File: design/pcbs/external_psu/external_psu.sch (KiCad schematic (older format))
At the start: 41 parts, among them J1 IEC 320-C14 socket, J2 DIN-4

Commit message: Updated PCB sheet info. Clarified licence in readme.
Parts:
- removed J1: IEC 320-C14 socket, symbol Connector_Generic:Conn_01x03
- removed J2: DIN-4, symbol Connector:DIN-4
- FB1: Done (none) -> Yes
- PS2: DigiKey (none) -> 945-3441-ND; Done (none) -> Yes
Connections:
- no-connect marks 3 -> 4
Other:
- note removed: "TODO: Add bushing\n(https://www.digikey.com.au/products/en/cables-wires-management/bushings-grommets/491?k=&pkeyword=&sv=0&pv716=10753&pv716=10888&pv716=12091&pv716=13319&sf=0&FV=845%7C323848%2C-8%7C491&quantity=&ColumnSort=1000011&page=1&stock=1&nstock=1&pageSize=25)\n\nAdd spiral wrap / techflex"
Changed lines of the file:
@@
 F 1 "RAC03-05SK" H 3150 5424 50  0000 C CNN
 F 2 "CONV_RAC03-05SK" H 2850 4550 50  0001 L BNN
-F 3 "Unavailable" H 3000 4400 50  0001 L BNN
+F 3 "https://www.recom-power.com/pdf/Powerline_AC-DC/RAC03-K.pdf" H 3000 4400 50  0001 L BNN
+F 4 "945-3441-ND" H 3150 5050 50  0001 C CNN "DigiKey"
+F 5 "Yes" H 3150 5050 50  0001 C CNN "Done"
 	1    3150 5050
 	1    0    0    -1
@@
 	7800 3550 7550 3550
 $Comp
-L Connector_Generic:Conn_01x03 J1
+L Connector_Generic:Conn_01x03 #J1
 U 1 1 5ED1F0ED
 P 1050 3550
-F 0 "J1" H 968 3867 50  0000 C CNN
+F 0 "#J1" H 968 3867 50  0000 C CNN
 F 1 "IEC 320-C14 socket" H 968 3776 50  0000 C CNN
 F 2 "" H 1050 3550 50  0001 C CNN
@@
 NoConn ~ 9850 4500
 NoConn ~ 9550 4500
-$Comp
-L Connector:DIN-4 J2
-U 1 1 5EED7BCF
-P 10350 4250
-F 0 "J2" V 10304 4020 50  0000 R CNN
-F 1 "DIN-4" V 10395 4020 50  0000 R CNN
-F 2 "" H 10350 4250 50  0001 C CNN
-F 3 "https://domino2.kycon.com/website/Tools/assemblyvideos/KPPX/KPPX%20Assembly%20instruction.pdf" H 10350 4250 50  0001 C CNN
-F 4 "2092-KPPX-4P-ND" V 10350 4250 50  0001 C CNN "DigiKey"
-	1    10350 4250
-	0    -1   1    0
-$EndComp
 Text Notes 9350 4900 0    50   ~ 0
 Ferrite bead around power \ncable on DAC end
@@
 	7400 3250 7800 3250
 Wire Wire Line
-	10050 4150 10050 4250
-Wire Wire Line
-	10050 4350 10050 4300
-Wire Wire Line
-	10350 3950 10000 3950
-Wire Wire Line
-	10000 3950 10000 4200
-Wire Wire Line
 	8350 3350 7800 3350
 Wire Wire Line
@@
 Wire Wire Line
 	7800 3250 7850 3250
-Wire Wire Line
-	10350 4550 10000 4550
-Wire Wire Line
-	10000 4550 10000 4350
 $Comp
 L Device:Ferrite_Bead FB1
@@
 F 3 "~" H 9700 4500 50  0001 C CNN
 F 4 "240-2497-ND" H 9700 4500 50  0001 C CNN "DigiKey"
+F 5 "Yes" H 9700 4500 50  0001 C CNN "Done"
 	1    9700 4500
 	0    1    1    0
 $EndComp
 Wire Wire Line
-	7550 3550 7550 4250
-Wire Wire Line
-	8350 4200 10000 4200
-Wire Wire Line
-	8350 3350 8350 4200
-Wire Wire Line
-	7800 4300 10050 4300
-Wire Wire Line
-	7400 3850 7800 3850
-Wire Wire Line
-	10050 4250 7550 4250
-Connection ~ 7550 4250
-Wire Wire Line
-	7550 4250 7550 5250
-Wire Wire Line
 	7400 4850 7800 4850
-Wire Wire Line
-	7800 4300 7800 3850
-Connection ~ 7800 3850
-Wire Wire Line
-	7800 3850 7850 3850
 Wire Wire Line
 	7800 4350 7800 4850
@@
 Text Notes 1150 2750 0    50   ~ 0
 Enclosure
-Text Notes 8250 5400 0    50   ~ 0
-TODO: Add bushing\n(https://www.digikey.com.au/products/en/cables-wires-management/bushings-grommets/491?k=&pkeyword=&sv=0&pv716=10753&pv716=10888&pv716=12091&pv716=13319&sf=0&FV=845%7C323848%2C-8%7C491&quantity=&ColumnSort=1000011&page=1&stock=1&nstock=1&pageSize=25)\n\nAdd spiral wrap / techflex
+$Comp
+L Connector:XLR5 #J2
+U 1 1 5EF8330A
+P 10350 4250
+F 0 "#J2" V 10396 4478 50  0000 L CNN
+F 1 "XLR5" V 10305 4478 50  0000 L CNN
+F 2 "" H 10350 4250 50  0001 C CNN
+F 3 "http://ioaudiotech.com/datasheet/IO-XLR5-BK.pdf" H 10350 4250 50  0001 C CNN
+F 4 "1937-1035-ND" V 10350 4250 50  0001 C CNN "DigiKey"
+F 5 "Yes" V 10350 4250 50  0001 C CNN "Done"
+	1    10350 4250
+	0    1    -1   0
+$EndComp
+Wire Wire Line
+	10000 4600 10350 4600
+Wire Wire Line
+	10350 4600 10350 4550
+Wire Wire Line
+	10000 4350 10000 4600
+Wire Wire Line
+	10250 4550 10050 4550
+Wire Wire Line
+	10050 4550 10050 4300
+Connection ~ 7550 4300
+Wire Wire Line
+	7550 4300 7550 5250
+Wire Wire Line
+	7550 3550 7550 4300
+Wire Wire Line
+	7550 4300 10050 4300
+Wire Wire Line
+	7400 3850 7800 3850
+Wire Wire Line
+	10050 4250 8350 4250
+Wire Wire Line
+	8350 3350 8350 4250
+Wire Wire Line
+	10250 3950 10050 3950
+Wire Wire Line
+	10050 3950 10050 4200
+Wire Wire Line
+	10050 4200 7800 4200
+Wire Wire Line
+	7800 4200 7800 3850
+Connection ~ 7800 3850
+Wire Wire Line
+	7800 3850 7850 3850
+NoConn ~ 10350 3950
 $EndSCHEMATC

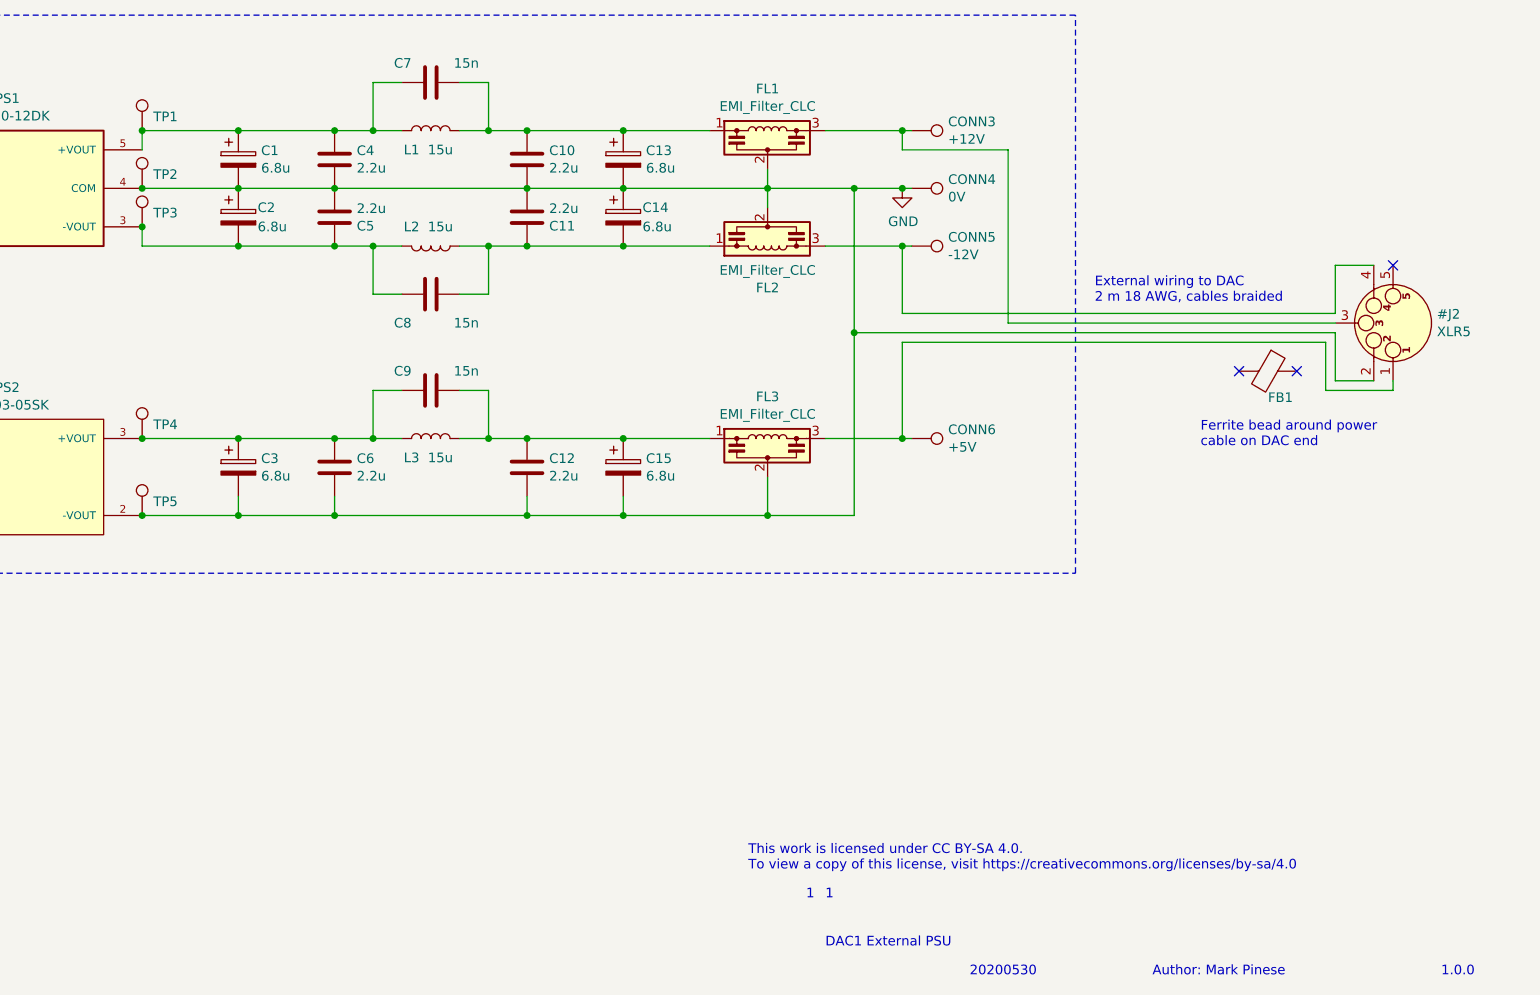
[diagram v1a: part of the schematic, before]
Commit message: Fixed title blocks. Added fab outputs.
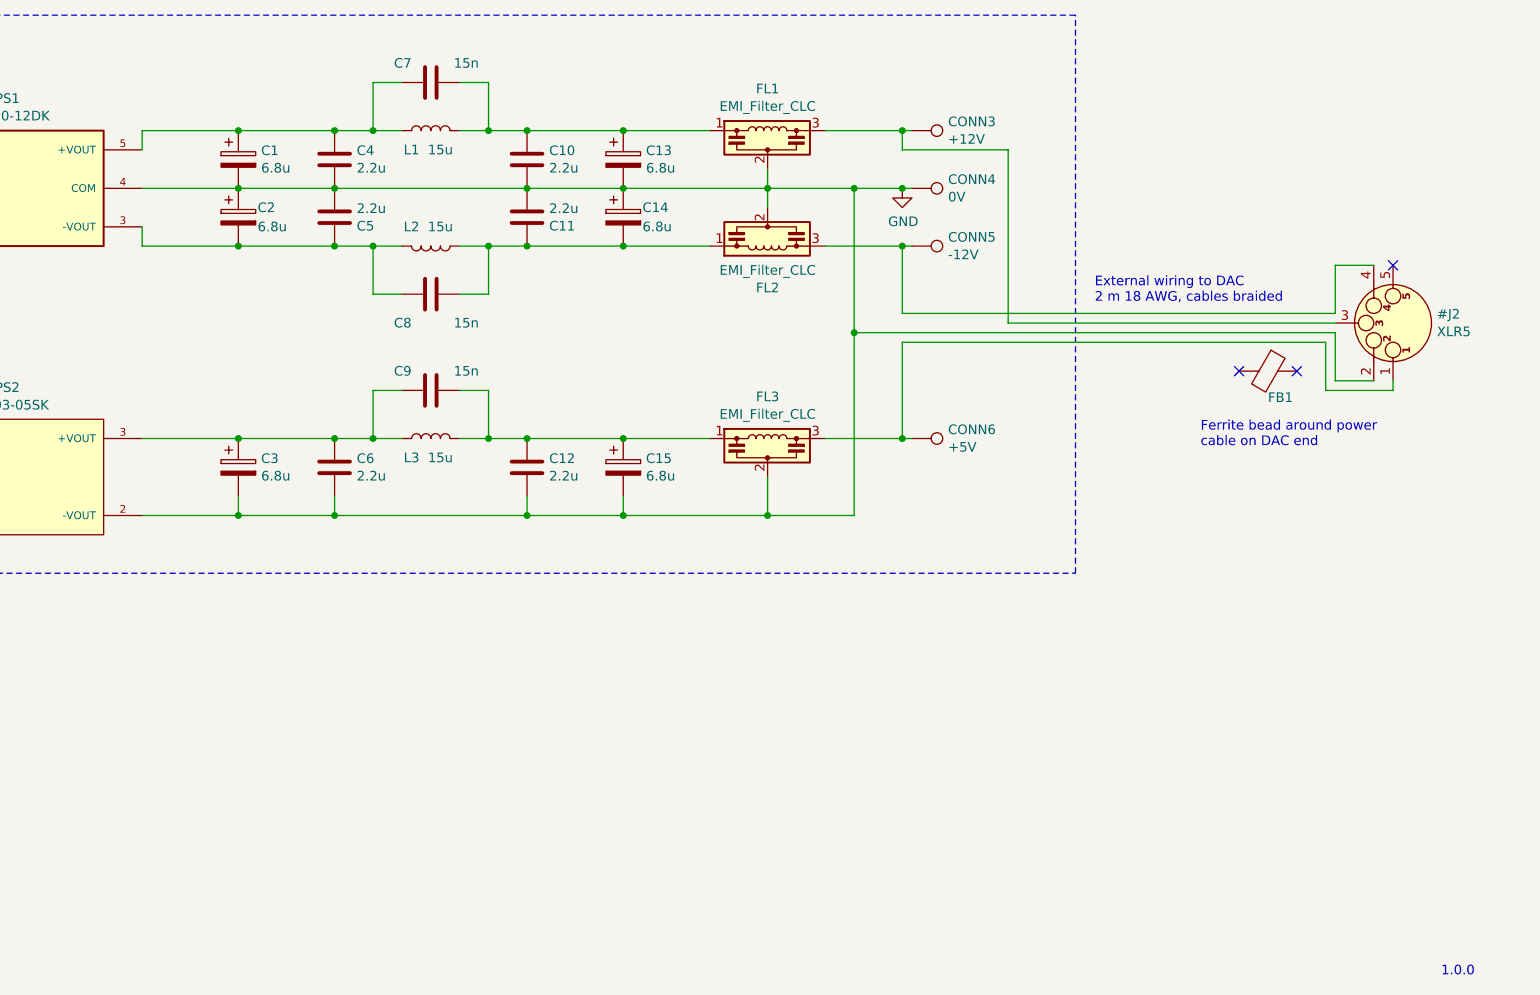
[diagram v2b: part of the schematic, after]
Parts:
- removed TP1, TP2, TP3, TP4, TP5: TestPoint, TestPoint:TestPoint_Pad_2.0x2.0mm, symbol Connector:TestPoint
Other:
- note removed: "1"
- note removed: "20200530"
- note removed: "Author: Mark Pinese"
- note removed: "DAC1 External PSU"
- note removed: "This work is licensed under CC BY-SA 4.0.\nTo view a copy of this license, visit https://creativecommons.org/licenses/by-sa/4.0"
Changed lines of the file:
@@
 encoding utf-8
 Sheet 1 1
-Title ""
-Date ""
-Rev ""
-Comp ""
-Comment1 ""
-Comment2 ""
+Title "DAC1 External PSU"
+Date "2020-06-27"
+Rev "1.0.0"
+Comp "© Mark Pinese 2020"
+Comment1 "To view a copy of this license, visit https://creativecommons.org/licenses/by/4.0"
+Comment2 "This work is licensed under CC BY 4.0."
 Comment3 ""
 Comment4 ""
@@
 	0    -1   -1   0
 $EndComp
-Text Notes 7400 7500 0    50   ~ 0
-DAC1 External PSU
 Text Notes 10600 7650 0    50   ~ 0
 1.0.0
-Text Notes 8150 7650 0    50   ~ 0
-20200530
-Text Notes 7300 7250 0    50   ~ 0
-1
-Text Notes 7400 7250 0    50   ~ 0
-1
-Text Notes 7000 7100 0    50   ~ 0
-This work is licensed under CC BY-SA 4.0.\nTo view a copy of this license, visit https://creativecommons.org/licenses/by-sa/4.0
-Text Notes 9100 7650 0    50   ~ 0
-Author: Mark Pinese
 Text Notes 850  3850 0    50   ~ 0
 Panel mounted
-$Comp
-L Connector:TestPoint TP1
-U 1 1 5ED7EA2A
-P 3850 3250
-F 0 "TP1" H 3908 3322 50  0000 L CNN
-F 1 "TestPoint" H 3908 3277 50  0001 L CNN
-F 2 "TestPoint:TestPoint_Pad_2.0x2.0mm" H 4050 3250 50  0001 C CNN
-F 3 "~" H 4050 3250 50  0001 C CNN
-	1    3850 3250
-	1    0    0    -1
-$EndComp
-Connection ~ 3850 3250
-$Comp
-L Connector:TestPoint TP2
-U 1 1 5ED8021F
-P 3850 3550
-F 0 "TP2" H 3908 3622 50  0000 L CNN
-F 1 "TestPoint" H 3908 3577 50  0001 L CNN
-F 2 "TestPoint:TestPoint_Pad_2.0x2.0mm" H 4050 3550 50  0001 C CNN
-F 3 "~" H 4050 3550 50  0001 C CNN
-	1    3850 3550
-	1    0    0    -1
-$EndComp
-Connection ~ 3850 3550
-$Comp
-L Connector:TestPoint TP3
-U 1 1 5ED8096F
-P 3850 3750
-F 0 "TP3" H 3908 3822 50  0000 L CNN
-F 1 "TestPoint" H 3908 3777 50  0001 L CNN
-F 2 "TestPoint:TestPoint_Pad_2.0x2.0mm" H 4050 3750 50  0001 C CNN
-F 3 "~" H 4050 3750 50  0001 C CNN
-	1    3850 3750
-	1    0    0    -1
-$EndComp
-Connection ~ 3850 3750
-$Comp
-L Connector:TestPoint TP5
-U 1 1 5ED80DD9
-P 3850 5250
-F 0 "TP5" H 3908 5322 50  0000 L CNN
-F 1 "TestPoint" H 3908 5277 50  0001 L CNN
-F 2 "TestPoint:TestPoint_Pad_2.0x2.0mm" H 4050 5250 50  0001 C CNN
-F 3 "~" H 4050 5250 50  0001 C CNN
-	1    3850 5250
-	1    0    0    -1
-$EndComp
-$Comp
-L Connector:TestPoint TP4
-U 1 1 5ED815D8
-P 3850 4850
-F 0 "TP4" H 3908 4922 50  0000 L CNN
-F 1 "TestPoint" H 3908 4877 50  0001 L CNN
-F 2 "TestPoint:TestPoint_Pad_2.0x2.0mm" H 4050 4850 50  0001 C CNN
-F 3 "~" H 4050 4850 50  0001 C CNN
-	1    3850 4850
-	1    0    0    -1
-$EndComp
-Connection ~ 3850 4850
-Connection ~ 3850 5250
 $Bitmap
 Pos 10050 1500

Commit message: Misc updates
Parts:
- removed FB1: ~, symbol Device:Ferrite_Bead
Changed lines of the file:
@@
 	7800 3250 7850 3250
 $Comp
-L Device:Ferrite_Bead FB1
+L Device:Ferrite_Bead #FB1
 U 1 1 5EED238E
 P 9700 4500
-F 0 "FB1" V 9837 4500 50  0000 L CNN
+F 0 "#FB1" V 9837 4500 50  0000 L CNN
 F 1 "~" H 9837 4455 50  0000 L CNN
 F 2 "" V 9630 4500 50  0001 C CNN
